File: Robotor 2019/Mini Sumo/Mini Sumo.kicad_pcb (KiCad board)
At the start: 2 copper layers, 80.5 x 99.7 mm, 78 parts, among them J1 Conn_01x03_Male, J2 Conn_01x04_Female, J3 USB_B_Mini, J4 Conn_01x01, J5 Conn_01x02, J6 Conn_01x01, M1 Motor_DC, M2 Motor_DC, SW1 SW_Push, SW2 SW_Push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

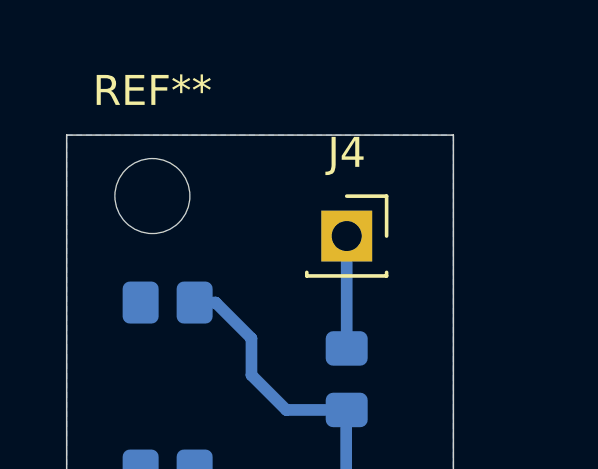
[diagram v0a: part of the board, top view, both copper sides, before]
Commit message: Schemele nu au nicio schimbare, doar am miscat putin textul sa se vada bine la imprimanta.
Programul am mai schimbat variabilele si vreau sa vad daca merge bine.
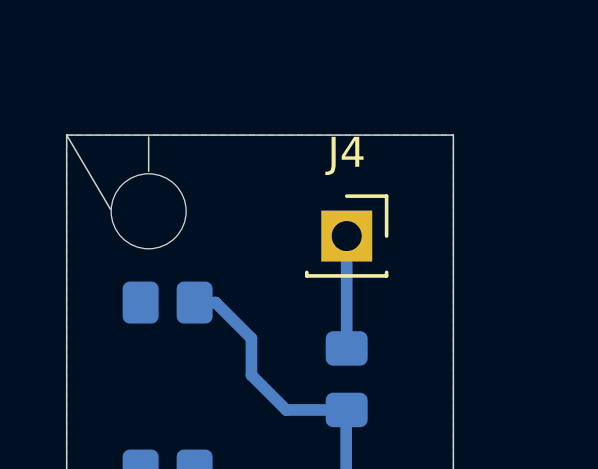
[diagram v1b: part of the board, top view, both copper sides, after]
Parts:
- REF**: moved to B.Cu
- moved REF** 0.52 mm to (123.5, 51.4)
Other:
- outline, holes or cut-outs redrawn
